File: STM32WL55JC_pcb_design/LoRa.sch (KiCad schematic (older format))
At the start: 24 parts

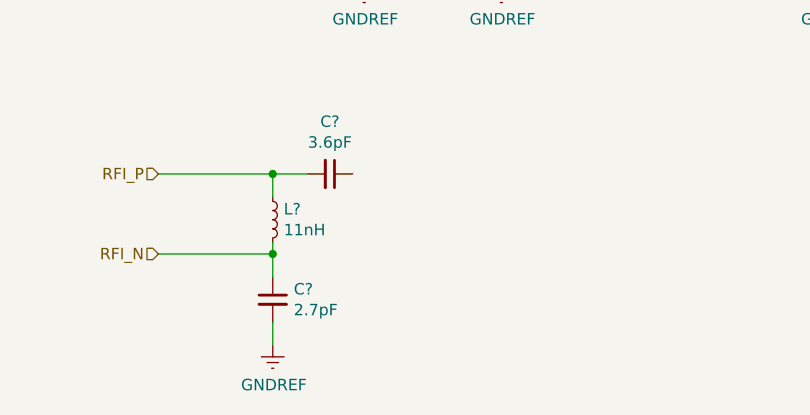
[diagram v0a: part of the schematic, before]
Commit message: Add missing cap on LoRa.sch
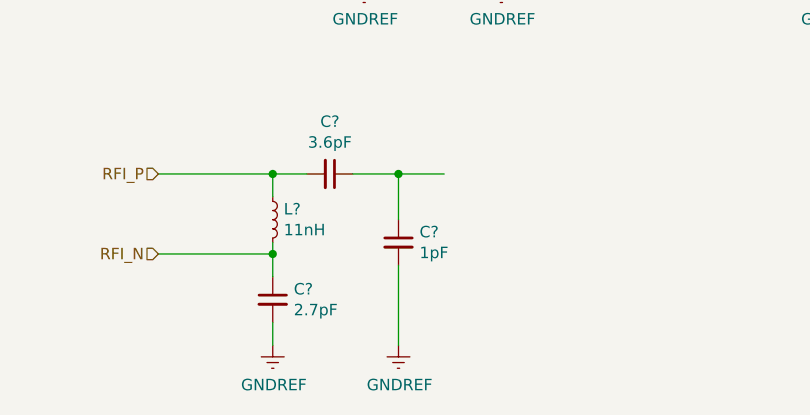
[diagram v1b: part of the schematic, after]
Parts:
- added C?: 1pF, symbol Device:C_Small
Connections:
- wire segments 55 -> 59
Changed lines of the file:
@@
 $Descr A4 11693 8268
 encoding utf-8
-Sheet 5 7
+Sheet 4 7
 Title ""
 Date ""
@@
 Wire Wire Line
 	6000 3650 6450 3650
+Wire Wire Line
+	5350 4900 5550 4900
+Wire Wire Line
+	5550 4900 5550 5100
+Connection ~ 5550 4900
+Wire Wire Line
+	5550 4900 5750 4900
+$Comp
+L Device:C_Small C?
+U 1 1 6166D0A0
+P 5550 5200
+F 0 "C?" H 5642 5246 50  0000 L CNN
+F 1 "1pF" H 5642 5155 50  0000 L CNN
+F 2 "" H 5550 5200 50  0001 C CNN
+F 3 "~" H 5550 5200 50  0001 C CNN
+	1    5550 5200
+	1    0    0    -1
+$EndComp
+Wire Wire Line
+	5550 5300 5550 5650
+$Comp
+L power:GNDREF #PWR?
+U 1 1 6166E9E7
+P 5550 5650
+F 0 "#PWR?" H 5550 5400 50  0001 C CNN
+F 1 "GNDREF" H 5555 5477 50  0000 C CNN
+F 2 "" H 5550 5650 50  0001 C CNN
+F 3 "" H 5550 5650 50  0001 C CNN
+	1    5550 5650
+	1    0    0    -1
+$EndComp
 $EndSCHEMATC

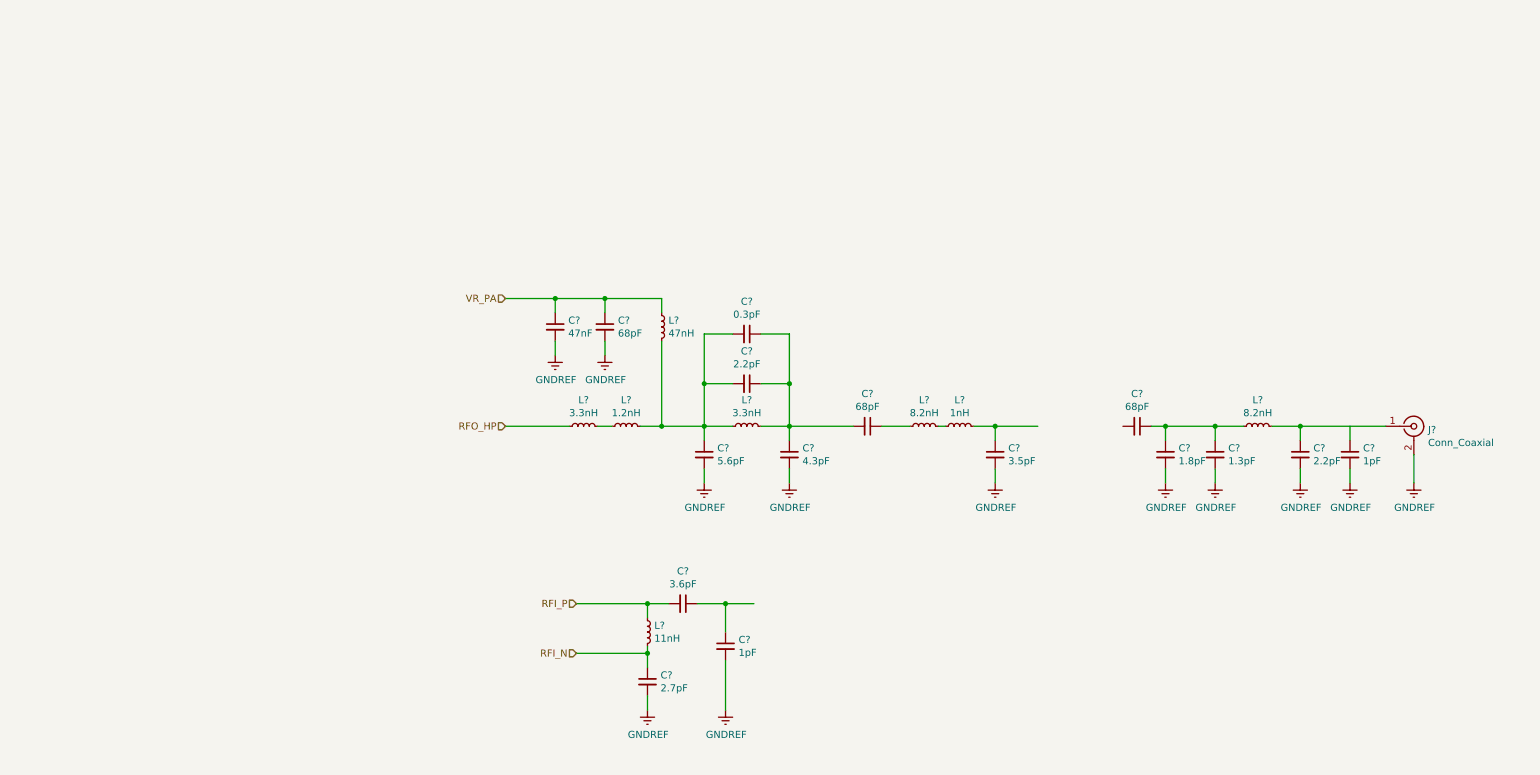
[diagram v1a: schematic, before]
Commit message: Finish RF matching network
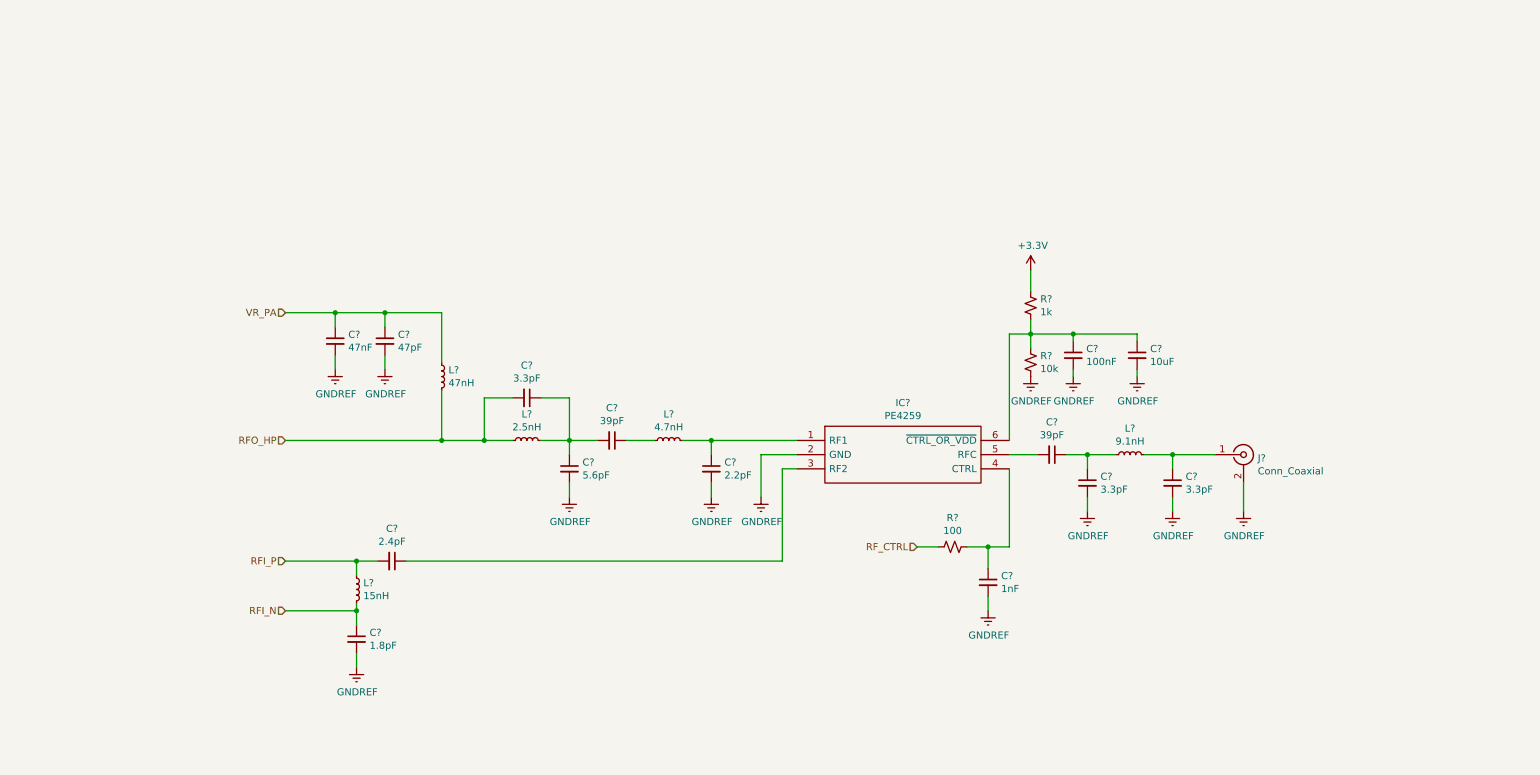
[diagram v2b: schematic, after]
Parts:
- removed C?: 5.6pF, symbol Device:C_Small
- removed C?: 0.3pF, symbol Device:C_Small
- removed C?: 1.8pF, symbol Device:C_Small
- removed C? (x2): 1pF, symbol Device:C_Small
- removed L?: 3.3nH, symbol Device:L_Small
- removed L?: 1nH, symbol Device:L_Small
- removed L?: 1.2nH, symbol Device:L_Small
- added C?: 100nF, symbol Device:C_Small
- added C?: 10uF, symbol Device:C_Small
- added C?: 1nF, symbol Device:C_Small
- added IC?: PE4259, SOT65P210X110-6N, symbol PE4259:PE4259
- added R?: 10k, symbol Device:R_Small_US
- added R?: 1k, symbol Device:R_Small_US
- added R?: 100, symbol Device:R_Small_US
- C?: value 68pF -> 47pF
- C? (x2): value 2.2pF -> 3.3pF
- C?: value 4.3pF -> 5.6pF
- C? (x2): value 68pF -> 39pF
- C?: value 3.5pF -> 2.2pF
- C?: value 3.6pF -> 2.4pF
- C?: value 2.7pF -> 1.8pF
- C?: value 1.3pF -> 3.3pF
- L?: value 3.3nH -> 2.5nH
- L?: value 8.2nH -> 4.7nH
- L?: value 11nH -> 15nH
- L?: value 8.2nH -> 9.1nH
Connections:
- net labels added: +3.3V, RF_CTRL
- wire segments 59 -> 64
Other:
- moved on the sheet: C?, J?, L?

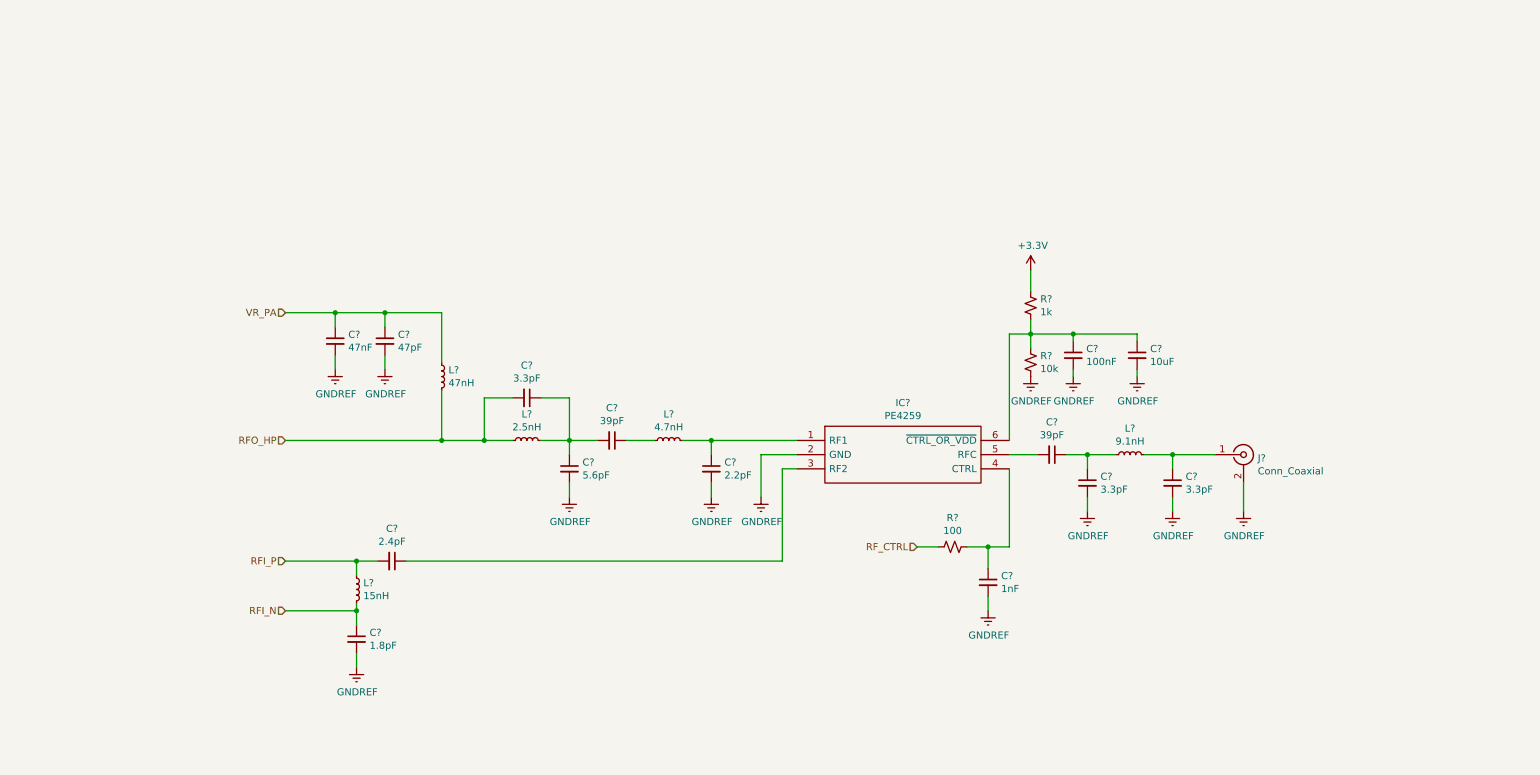
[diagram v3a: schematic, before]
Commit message: Finish component selection and footprint assignment
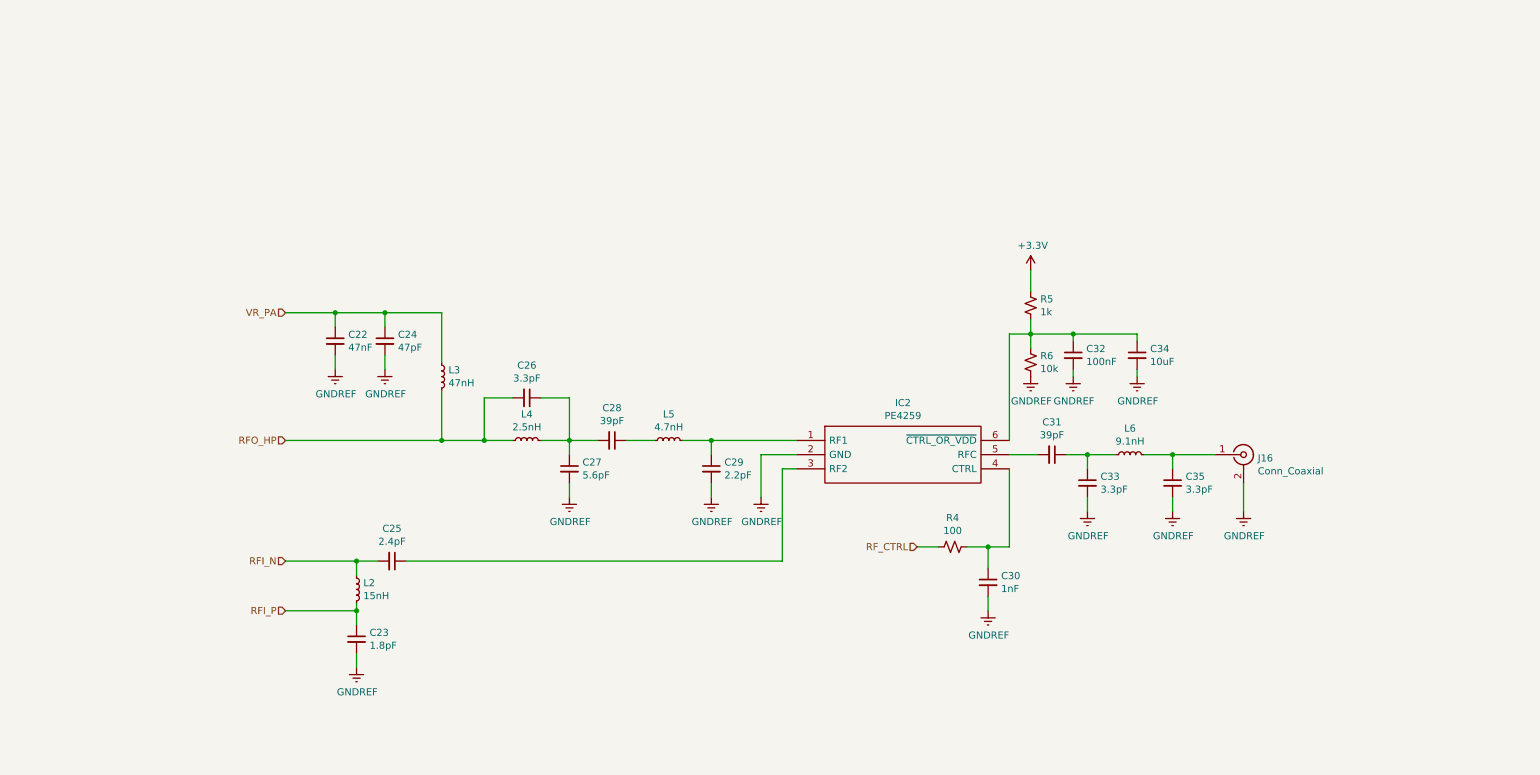
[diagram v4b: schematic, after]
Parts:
- C22, C23, C24, C26, C27, C28, C30, C31, C32, C33, C34, C35: renamed from C?; footprint (none) -> Capacitor_SMD:C_0805_2012Metric
- C25: renamed from C?; footprint (none) -> Capacitor_SMD:C_0603_1608Metric
- C29: renamed from C?; footprint (none) -> Capacitor_SMD:C_0402_1005Metric
- IC2: renamed from IC?; footprint SOT65P210X110-6N -> PE4259:SOT65P210X110-6N
- J16: renamed from J?; footprint (none) -> Connector_Coaxial:SMA_Amphenol_901-144_Vertical
- L2: renamed from L?; footprint (none) -> Inductor_SMD:L_01005_0402Metric
- L3, L5: renamed from L?; footprint (none) -> Inductor_SMD:L_0805_2012Metric
- L4, L6: renamed from L?; footprint (none) -> Inductor_SMD:L_0402_1005Metric
- R4, R5, R6: renamed from R?; footprint (none) -> Resistor_SMD:R_0805_2012Metric
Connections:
- net RFI_N: now also C25.2, L2.1; no longer C23.1, L2.2
- net RFI_P: now also C23.1, L2.2; no longer C25.2, L2.1

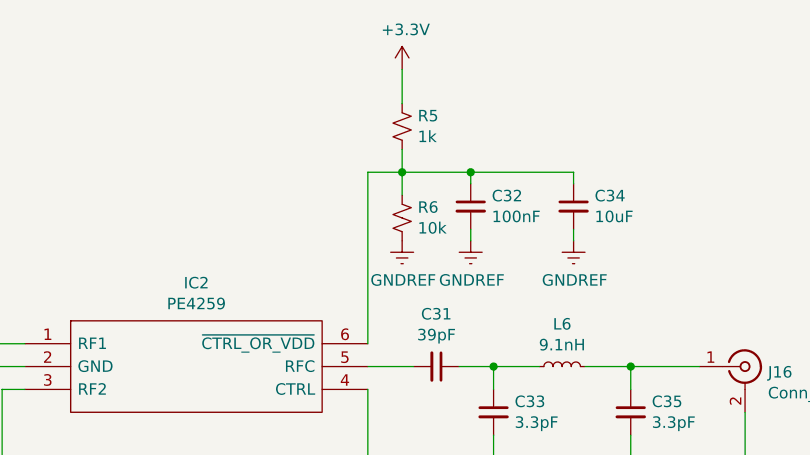
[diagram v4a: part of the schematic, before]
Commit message: Initial pcb layout
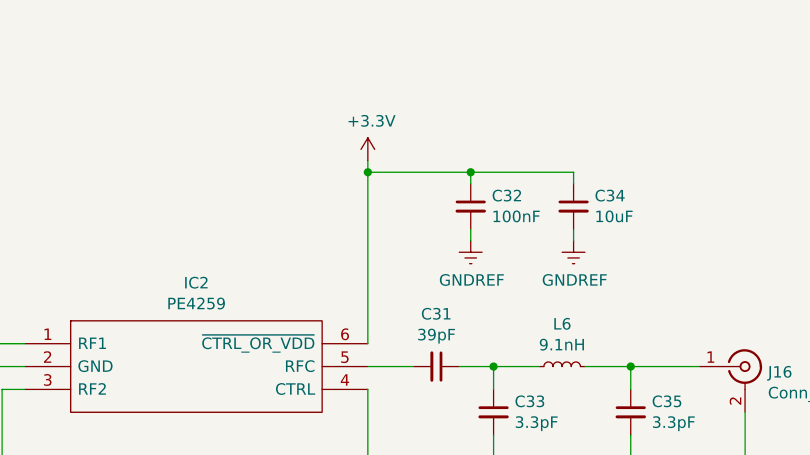
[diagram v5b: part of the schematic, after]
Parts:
- removed R5: 1k, Resistor_SMD:R_0805_2012Metric, symbol Device:R_Small_US
- removed R6: 10k, Resistor_SMD:R_0805_2012Metric, symbol Device:R_Small_US
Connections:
- net +3V3: now also C32.1, C34.1, IC2.6 (~CTRL_OR_VDD)
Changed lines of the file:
@@
 	7550 3850 7750 3850
-$Comp
-L Device:R_Small_US R6
-U 1 1 6159723D
-P 7700 3200
-F 0 "R6" H 7768 3246 50  0000 L CNN
-F 1 "10k" H 7768 3155 50  0000 L CNN
-F 2 "Resistor_SMD:R_0805_2012Metric" H 7700 3200 50  0001 C CNN
-F 3 "~" H 7700 3200 50  0001 C CNN
-	1    7700 3200
-	1    0    0    -1
-$EndComp
-$Comp
-L Device:R_Small_US R5
-U 1 1 615977AA
-P 7700 2800
-F 0 "R5" H 7768 2846 50  0000 L CNN
-F 1 "1k" H 7768 2755 50  0000 L CNN
-F 2 "Resistor_SMD:R_0805_2012Metric" H 7700 2800 50  0001 C CNN
-F 3 "~" H 7700 2800 50  0001 C CNN
-	1    7700 2800
-	1    0    0    -1
-$EndComp
-Wire Wire Line
-	7700 2900 7700 3000
-Wire Wire Line
-	7700 2700 7700 2550
 $Comp
 L power:GNDREF #PWR0137
@@
 $EndComp
 Wire Wire Line
-	7700 3000 7550 3000
-Connection ~ 7700 3000
-Wire Wire Line
-	7700 3000 7700 3100
-$Comp
-L power:GNDREF #PWR0139
-U 1 1 615AED0A
-P 7700 3300
-F 0 "#PWR0139" H 7700 3050 50  0001 C CNN
-F 1 "GNDREF" H 7705 3127 50  0000 C CNN
-F 2 "" H 7700 3300 50  0001 C CNN
-F 3 "" H 7700 3300 50  0001 C CNN
-	1    7700 3300
-	1    0    0    -1
-$EndComp
-Wire Wire Line
 	7550 3000 7550 3750
 $Comp
 L power:+3.3V #PWR?
 U 1 1 615B53A5
-P 7700 2550
+P 7550 2950
 AR Path="/615B53A5" Ref="#PWR?"  Part="1"
 AR Path="/613C9E7C/615B53A5" Ref="#PWR0140"  Part="1"
-F 0 "#PWR0140" H 7700 2400 50  0001 C CNN
-F 1 "+3.3V" H 7715 2723 50  0000 C CNN
-F 2 "" H 7700 2550 50  0001 C CNN
-F 3 "" H 7700 2550 50  0001 C CNN
-	1    7700 2550
+F 0 "#PWR0140" H 7550 2800 50  0001 C CNN
+F 1 "+3.3V" H 7565 3123 50  0000 C CNN
+F 2 "" H 7550 2950 50  0001 C CNN
+F 3 "" H 7550 2950 50  0001 C CNN
+	1    7550 2950
 	1    0    0    -1
 $EndComp
@@
 	1    0    0    -1
 $EndComp
-Wire Wire Line
-	7700 3000 8000 3000
 $Comp
 L Device:C_Small C32
@@
 Wire Wire Line
 	7400 4850 7400 4950
+Wire Wire Line
+	7550 3000 8000 3000
+Wire Wire Line
+	7550 2950 7550 3000
+Connection ~ 7550 3000
 $EndSCHEMATC
